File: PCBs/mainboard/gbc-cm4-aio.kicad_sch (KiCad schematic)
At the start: 128 parts, among them J1 Conn_01x40, J2 AudioJack2_Ground_Switch, J4 DM3D-SF, J6 Conn_01x11, J7 Conn_01x02, P1 USB_C_Plug_USB2.0, Q1 2N7002E, Q1 AO4407C, SW1 SW_Push, SW3 SW_Push_Dual_x2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

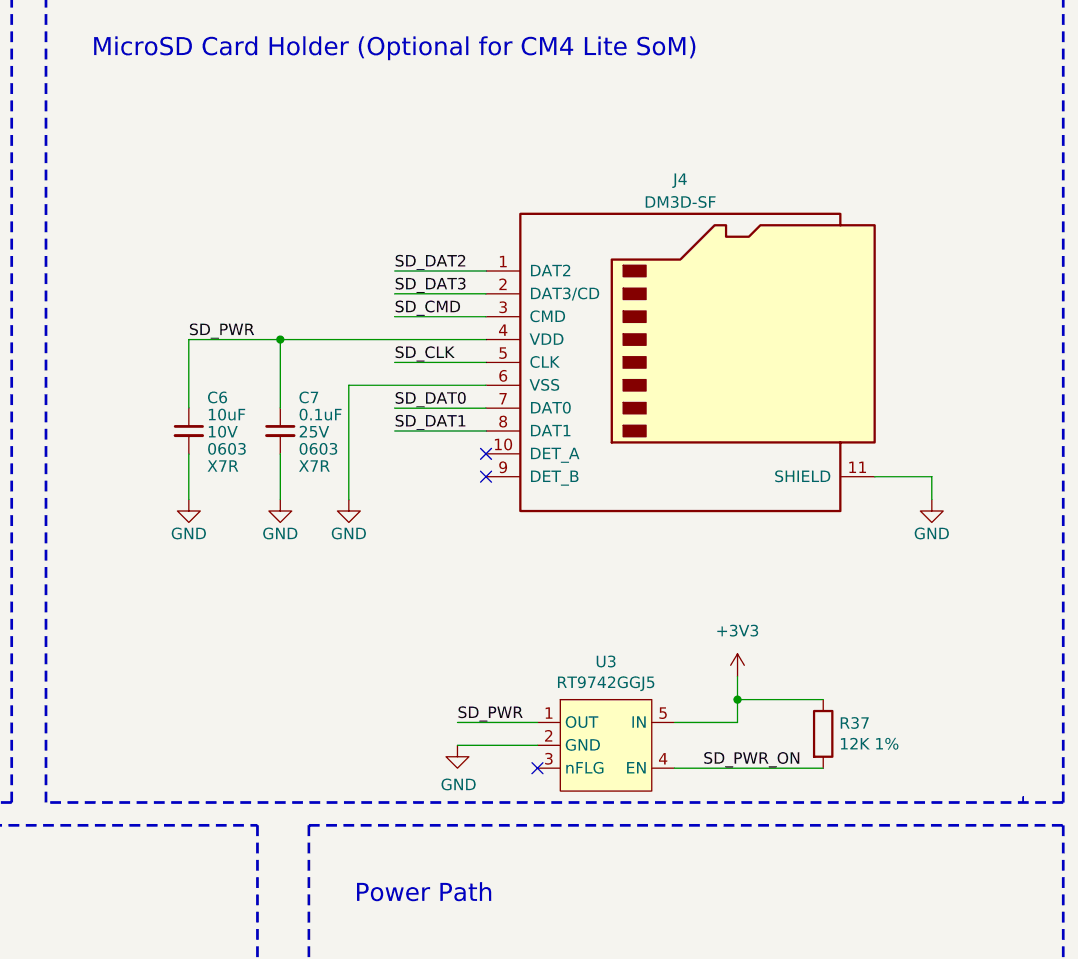
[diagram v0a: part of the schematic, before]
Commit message: revise sd card and lcd driver placement
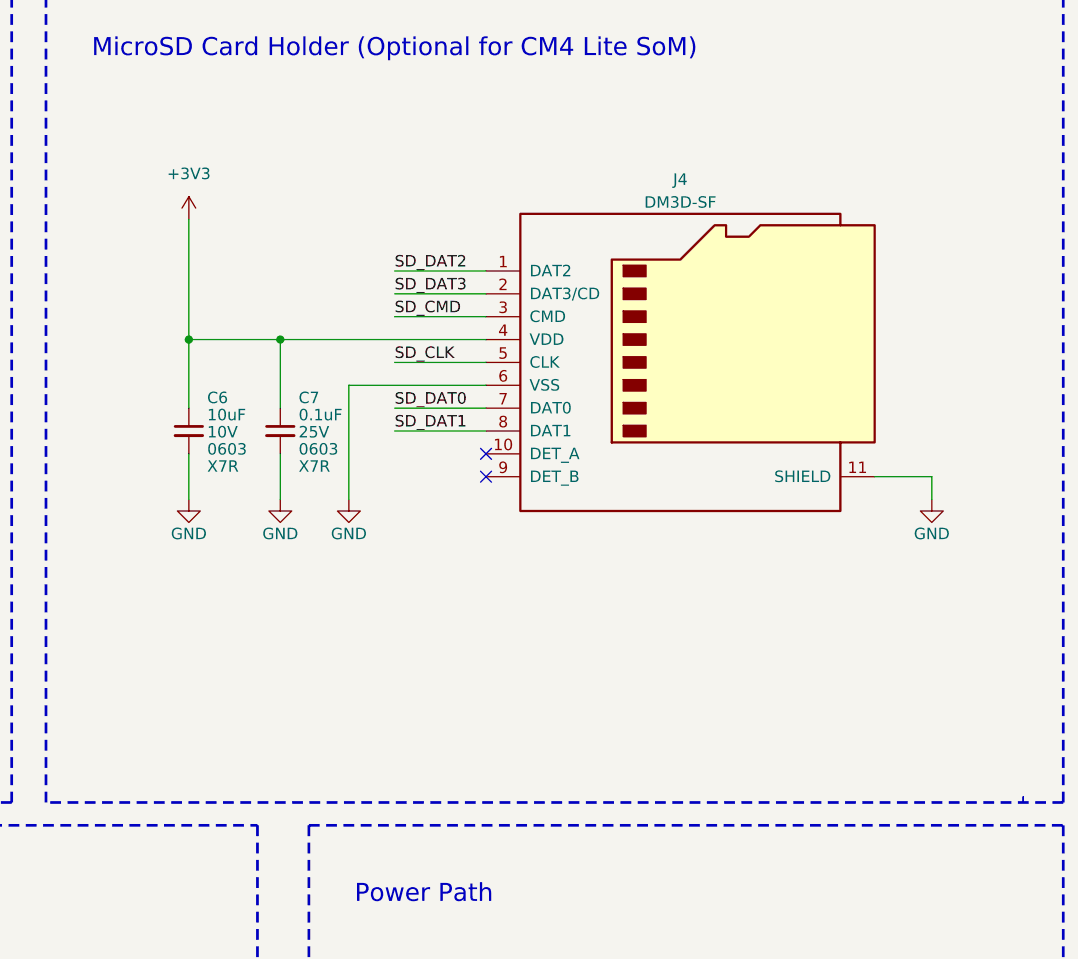
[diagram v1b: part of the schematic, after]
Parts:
- removed R37: 12K 1%, Resistor_SMD:R_0603_1608Metric_Pad0.98x0.95mm_HandSolder, symbol Device:R
- removed U3: RT9742GGJ5, Package_TO_SOT_SMD:SOT-23-5, symbol CM4IO:RT9742GGJ5
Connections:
- net SD_PWR is gone; now on net +3V3: C6.1, C7.1, J4.4 (VDD)
- no-connect marks 100 -> 99

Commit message: move i2c bus to i2c1
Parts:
- removed JP1, JP2: ~, Jumper:SolderJumper-2_P1.3mm_Open_RoundedPad1.0x1.5mm, symbol cm4-carrier-net-rescue:Jumper_NC_Small-Device
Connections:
- net SCL0: no longer R2.2, SCL1.1, U4.7 (SCL)
- net SDA0: no longer R1.2, SDA1.1, U4.8 (SDA)
- net SCL1: now reaches Module1.56 (GPIO3)
- net SCL1: now also R2.2, SCL1.1, U4.7 (SCL)
- net SDA1: now reaches Module1.58 (GPIO2)
- net SDA1: now also R1.2, SDA1.1, U4.8 (SDA)

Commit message: revise inductors packages
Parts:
- L3: footprint Inductor_SMD:L_6.3x6.3_H3 -> Inductor_SMD:L_Changjiang_FNR3015S
- L4: footprint Inductor_SMD:L_6.3x6.3_H3 -> Inductor_SMD:L_Changjiang_FNR4020S
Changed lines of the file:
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@@
 			)
 		)
-		(property "Footprint" "Inductor_SMD:L_6.3x6.3_H3"
+		(property "Footprint" "Inductor_SMD:L_Changjiang_FNR3015S"
 			(at 60.96 138.43 0)
 			(effects
@@
 			)
 		)
-		(property "Footprint" "Inductor_SMD:L_6.3x6.3_H3"
+		(property "Footprint" "Inductor_SMD:L_Changjiang_FNR4020S"
 			(at 508.635 117.475 0)
 			(effects

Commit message: minor optimizations
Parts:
- removed R14, R15: TBD, Resistor_SMD:R_0603_1608Metric, symbol Device:R
- removed R28, R29: 10K, Resistor_SMD:R_0603_1608Metric, symbol Device:R
- removed R7, R8: 2.2K 1%, Resistor_SMD:R_0603_1608Metric, symbol Device:R
- R26: value 732K -> 680K
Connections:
- net GND: now also U10.6 (MODE)
- net VBUS: now also U9.2 (VPCC)
- net VIN: now also U10.5 (EN)
- net GLOBAL_EN: no longer names the net of Module1.99 (Global_EN)
- net SCL0: no longer names the net of Module1.80 (SCL0)
- net SDA0: no longer names the net of Module1.82 (SDA0)
- net SD_PWR_ON: no longer names the net of Module1.75 (SD_PWR_ON)

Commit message: minor optimizations
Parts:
- removed R4, R6: 10k, Resistor_SMD:R_0603_1608Metric, symbol Device:R
- L4: footprint Inductor_SMD:L_Changjiang_FNR4020S -> Inductor_SMD:L_Changjiang_FNR5030S
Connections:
- net +3V3: now also U1.3 (EN)
- net +5V: now also U7.5 (EN)
- net IP0 renamed CC1
- net IP1 renamed CC2
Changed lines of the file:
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@@
 	(wire
 		(pts
-			(xy 33.655 90.17) (xy 34.925 90.17)
-		)
-		(stroke
-			(width 0)
-			(type default)
-		)
-	)
-	(wire
-		(pts
 			(xy 365.125 224.155) (xy 381 224.155)
 		)
@@
 		)
 	)
+	(wire
+		(pts
+			(xy 33.655 90.17) (xy 43.815 90.17)
+		)
+		(stroke
+			(width 0)
+			(type default)
+		)
+	)
 	(polyline
 		(pts
@@
 	(wire
 		(pts
-			(xy 42.545 90.17) (xy 43.815 90.17)
-		)
-		(stroke
-			(width 0)
-			(type default)
-		)
-	)
-	(wire
-		(pts
 			(xy 534.67 54.61) (xy 543.56 54.61)
 		)
@@
 	(wire
 		(pts
-			(xy 41.91 49.53) (xy 43.18 49.53)
-		)
-		(stroke
-			(width 0)
-			(type default)
-		)
-	)
-	(wire
-		(pts
 			(xy 277.495 303.53) (xy 277.495 300.99)
 		)
@@
 	(wire
 		(pts
-			(xy 34.29 49.53) (xy 33.02 49.53)
+			(xy 33.02 49.53) (xy 43.18 49.53)
 		)
 		(stroke
@@
 		)
 	)
-	(label "IP1"
+	(label "CC2"
 		(at 532.13 213.995 0)
 		(fields_autoplaced yes)
@@
 		)
 	)
-	(label "IP1"
+	(label "CC2"
 		(at 514.35 244.475 0)
 		(fields_autoplaced yes)
@@
 		)
 	)
-	(label "IP0"
+	(label "CC1"
 		(at 514.35 239.395 0)
 		(fields_autoplaced yes)
@@
 		)
 	)
-	(label "IP0"
+	(label "CC1"
 		(at 532.13 211.455 0)
 		(fields_autoplaced yes)
@@
 	)
 	(symbol
-		(lib_id "Device:R")
-		(at 38.1 49.53 90)
-		(unit 1)
-		(exclude_from_sim no)
-		(in_bom yes)
-		(on_board yes)
-		(dnp no)
-		(property "Reference" "R6"
-			(at 38.1 54.61 90)
-			(effects
-				(font
-					(size 1.27 1.27)
-				)
-			)
-		)
-		(property "Value" "10k"
-			(at 38.1 52.07 90)
-			(effects
-				(font
-					(size 1.27 1.27)
-				)
-			)
-		)
-		(property "Footprint" "Resistor_SMD:R_0603_1608Metric"
-			(at 38.1 51.308 90)
-			(effects
-				(font
-					(size 1.27 1.27)
-				)
-				(hide yes)
-			)
-		)
-		(property "Datasheet" "~"
-			(at 38.1 49.53 0)
-			(effects
-				(font
-					(size 1.27 1.27)
-				)
-				(hide yes)
-			)
-		)
-		(property "Description" ""
-			(at 38.1 49.53 0)
-			(effects
-				(font
-					(size 1.27 1.27)
-				)
-				(hide yes)
-			)
-		)
-		(pin "1"
-		)
-		(pin "2"
-		)
-		(instances
-			(project "gbc-cm4-aio"
-				(path "/4dda0f32-68f6-467e-9c4a-af7e2b8a8793"
-					(reference "R6")
-					(unit 1)
-				)
-			)
-			(project "rpi-q5-adapter"
-				(path "/e618c82d-b530-40f1-81e4-eb7b21173688"
-					(reference "R3")
-					(unit 1)
-				)
-			)
-		)
-	)
-	(symbol
 		(lib_id "power:GND")
 		(at 118.745 125.095 0)
@@
 	)
 	(symbol
-		(lib_id "Device:R")
-		(at 38.735 90.17 90)
-		(unit 1)
-		(exclude_from_sim no)
-		(in_bom yes)
-		(on_board yes)
-		(dnp no)
-		(property "Reference" "R4"
-			(at 38.735 95.25 90)
-			(effects
-				(font
-					(size 1.27 1.27)
-				)
-			)
-		)
-		(property "Value" "10k"
-			(at 38.735 92.71 90)
-			(effects
-				(font
-					(size 1.27 1.27)
-				)
-			)
-		)
-		(property "Footprint" "Resistor_SMD:R_0603_1608Metric"
-			(at 38.735 91.948 90)
-			(effects
-				(font
-					(size 1.27 1.27)
-				)
-				(hide yes)
-			)
-		)
-		(property "Datasheet" "~"
-			(at 38.735 90.17 0)
-			(effects
-				(font
-					(size 1.27 1.27)
-				)
-				(hide yes)
-			)
-		)
-		(property "Description" ""
-			(at 38.735 90.17 0)
-			(effects
-				(font
-					(size 1.27 1.27)
-				)
-				(hide yes)
-			)
-		)
-		(pin "1"
-		)
-		(pin "2"
-		)
-		(instances
-			(project "gbc-cm4-aio"
-				(path "/4dda0f32-68f6-467e-9c4a-af7e2b8a8793"
-					(reference "R4")
-					(unit 1)
-				)
-			)
-			(project "rpi-q5-adapter"
-				(path "/e618c82d-b530-40f1-81e4-eb7b21173688"
-					(reference "R1")
-					(unit 1)
-				)
-			)
-		)
-	)
-	(symbol
 		(lib_id "Transistor_FET:2N7002E")
 		(at 324.485 231.775 0)
@@
 			)
 		)
-		(property "Footprint" "Inductor_SMD:L_Changjiang_FNR4020S"
+		(property "Footprint" "Inductor_SMD:L_Changjiang_FNR5030S"
 			(at 508.635 117.475 0)
 			(effects

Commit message: mainboard placement optimization
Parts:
- added C35: 10uF, PintryParts-Footprints:C_0603_1608Metric, symbol Device:C_Small
- added C41, C42: 0.1uF, PintryParts-Footprints:C_0603_1608Metric, symbol Device:C_Small
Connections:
- net +1V8: now also C35.1, C41.1
- net +5V: now also C42.1
- net GND: now also C35.2, C41.2, C42.2
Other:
- moved on the sheet: C1, C2

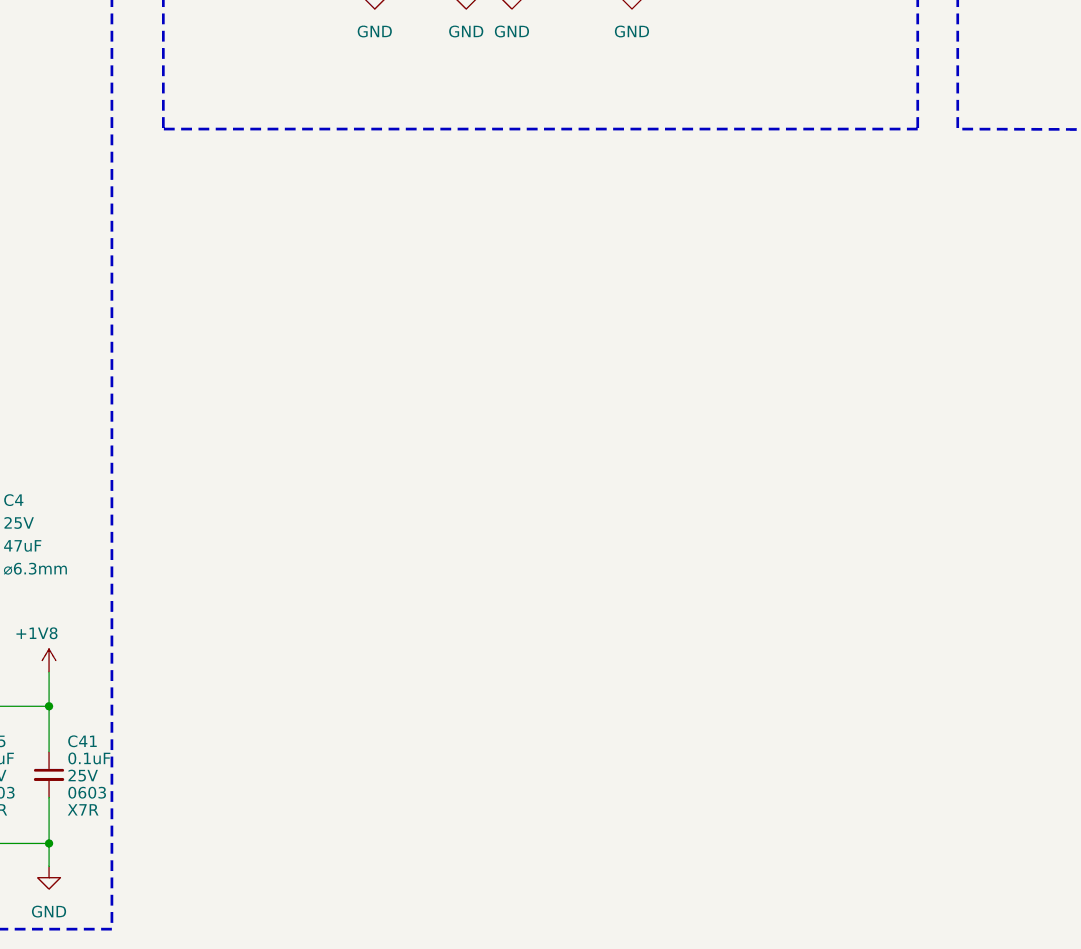
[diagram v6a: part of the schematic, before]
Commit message: added tactile switches
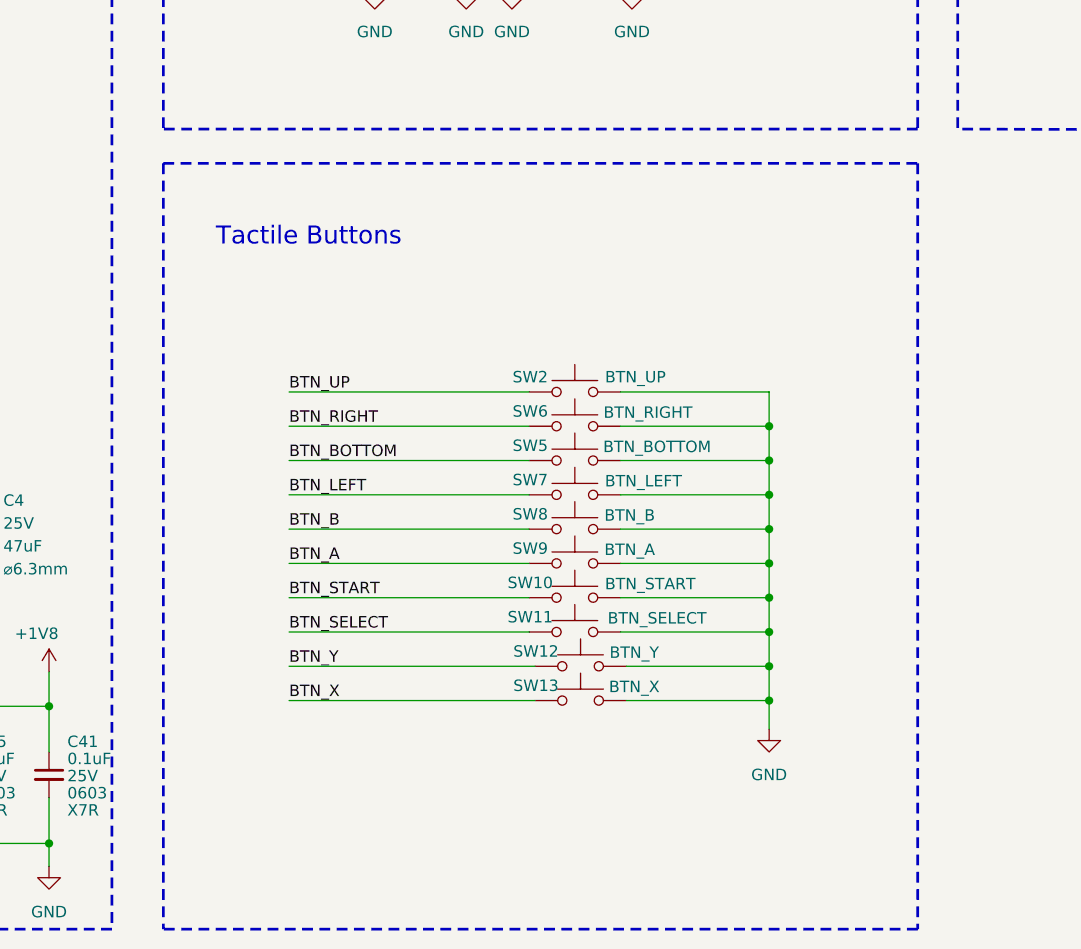
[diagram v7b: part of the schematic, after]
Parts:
- added SW10: BTN_START, Button_Switch_SMD:SKRMABE010, symbol Switch:SW_Push
- added SW11: BTN_SELECT, Button_Switch_SMD:SKRMABE010, symbol Switch:SW_Push
- added SW12: BTN_Y, Button_Switch_SMD:SKRMABE010, symbol Switch:SW_Push
- added SW13: BTN_X, Button_Switch_SMD:SKRMABE010, symbol Switch:SW_Push
- added SW2: BTN_UP, Button_Switch_SMD:SKRMABE010, symbol Switch:SW_Push
- added SW5: BTN_BOTTOM, Button_Switch_SMD:SKRMABE010, symbol Switch:SW_Push
- added SW6: BTN_RIGHT, Button_Switch_SMD:SKRMABE010, symbol Switch:SW_Push
- added SW7: BTN_LEFT, Button_Switch_SMD:SKRMABE010, symbol Switch:SW_Push
- added SW8: BTN_B, Button_Switch_SMD:SKRMABE010, symbol Switch:SW_Push
- added SW9: BTN_A, Button_Switch_SMD:SKRMABE010, symbol Switch:SW_Push
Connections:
- net BTN_A: now also SW9.1
- net BTN_B: now also SW8.1
- net BTN_BOTTOM: now also SW5.1
- net BTN_LEFT: now also SW7.1
- net BTN_RIGHT: now also SW6.1
- net BTN_SELECT: now also SW11.1
- net BTN_START: now also SW10.1
- net BTN_UP: now also SW2.1
- net BTN_X: now also SW13.1
- net BTN_Y: now also SW12.1
- net GND: now also SW10.2, SW11.2, SW12.2, SW13.2, SW2.2, SW5.2, SW6.2, SW7.2, SW8.2, SW9.2
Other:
- note added: "Tactile Buttons"
